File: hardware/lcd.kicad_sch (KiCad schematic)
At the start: 7 parts, among them J3 Conn_01x40, Q2 AO3400A

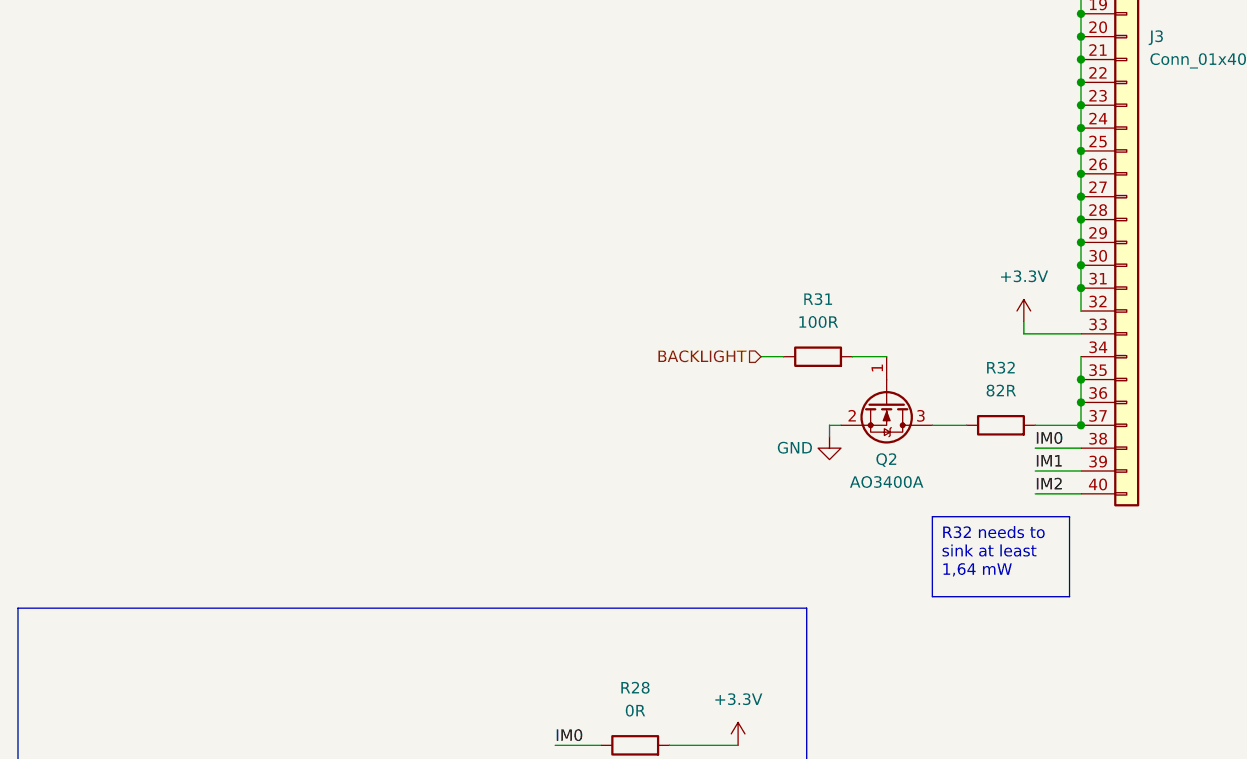
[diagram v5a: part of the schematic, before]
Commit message: Fix resistor value, fix error in schematic
Pin 37 was incorrectly bunched with the backlight LED cathodes, but is
actually a GND pin.
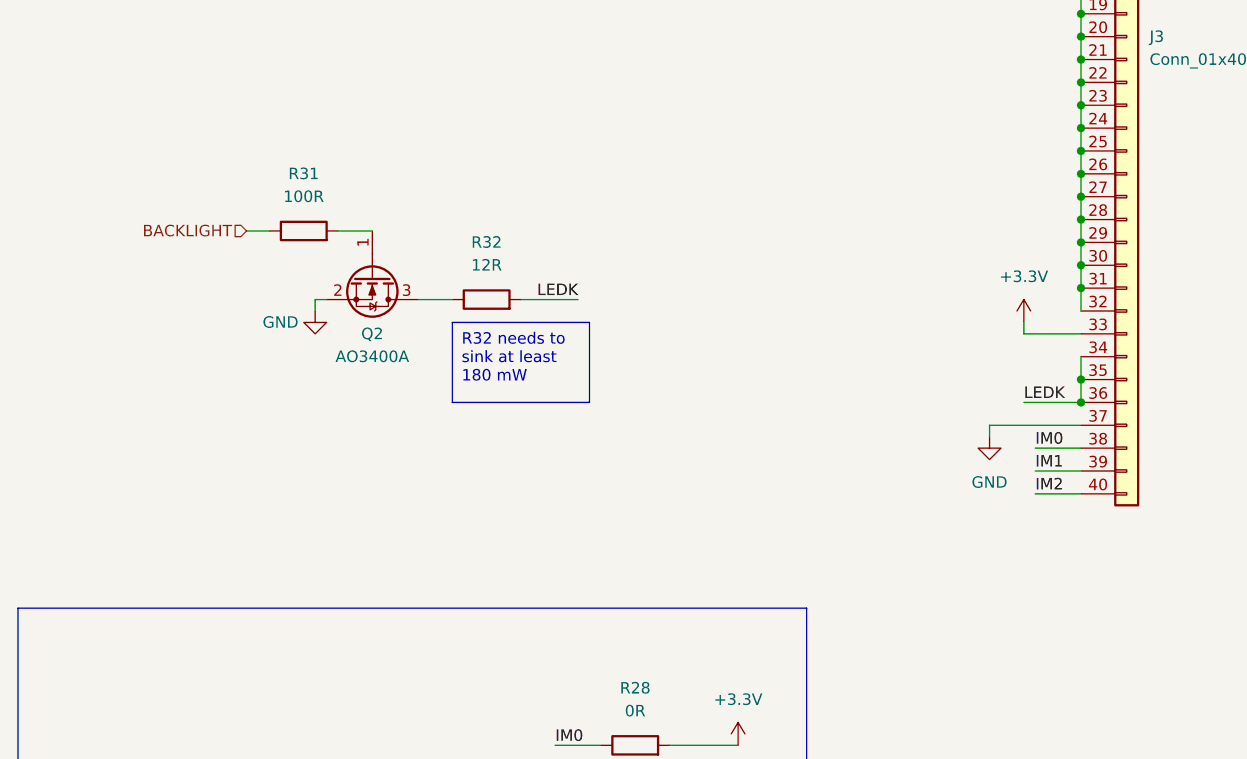
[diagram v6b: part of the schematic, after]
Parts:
- R32: value 82R -> 12R
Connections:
- net GND: now also J3.37 (Pin_37)
- net LEDK: now reaches J3.34 (Pin_34), J3.35 (Pin_35), J3.36 (Pin_36), R32.2
- net LEDK: no longer J3.37 (Pin_37)
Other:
- moved on the sheet: Q2, R31, R32
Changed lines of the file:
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@@
 	)
 	(junction
-		(at 133.35 129.54)
-		(diameter 0)
-		(color 0 0 0 0)
-	)
-	(junction
 		(at 133.35 109.22)
 		(diameter 0)
@@
 	)
 	(junction
-		(at 133.35 127)
+		(at 133.35 99.06)
 		(diameter 0)
 		(color 0 0 0 0)
 	)
 	(junction
-		(at 133.35 99.06)
+		(at 133.35 88.9)
 		(diameter 0)
 		(color 0 0 0 0)
 	)
 	(junction
-		(at 133.35 88.9)
+		(at 133.35 83.82)
 		(diameter 0)
 		(color 0 0 0 0)
 	)
 	(junction
-		(at 133.35 83.82)
+		(at 133.35 127)
 		(diameter 0)
 		(color 0 0 0 0)
@@
 	(wire
 		(pts
+			(xy 71.12 115.57) (xy 77.47 115.57)
+		)
+		(stroke
+			(width 0)
+			(type default)
+		)
+	)
+	(wire
+		(pts
 			(xy 118.11 60.96) (xy 118.11 66.04)
 		)
@@
 	(wire
 		(pts
-			(xy 116.84 129.54) (xy 120.65 129.54)
+			(xy 59.69 115.57) (xy 63.5 115.57)
 		)
 		(stroke
@@
 	(wire
 		(pts
+			(xy 123.19 129.54) (xy 133.35 129.54)
+		)
+		(stroke
+			(width 0)
+			(type default)
+		)
+	)
+	(wire
+		(pts
 			(xy 87.63 185.42) (xy 95.25 185.42)
 		)
@@
 	(wire
 		(pts
+			(xy 123.19 130.81) (xy 123.19 129.54)
+		)
+		(stroke
+			(width 0)
+			(type default)
+		)
+	)
+	(wire
+		(pts
 			(xy 133.35 93.98) (xy 133.35 96.52)
 		)
@@
 	(wire
 		(pts
-			(xy 130.81 55.88) (xy 133.35 55.88)
+			(xy 127 127) (xy 133.35 127)
 		)
 		(stroke
@@
 	(wire
 		(pts
-			(xy 88.9 175.26) (xy 88.9 176.53)
+			(xy 130.81 55.88) (xy 133.35 55.88)
 		)
 		(stroke
@@
 	(wire
 		(pts
-			(xy 87.63 175.26) (xy 88.9 175.26)
+			(xy 88.9 175.26) (xy 88.9 176.53)
 		)
 		(stroke
@@
 	(wire
 		(pts
-			(xy 106.68 129.54) (xy 105.41 129.54)
+			(xy 87.63 175.26) (xy 88.9 175.26)
 		)
 		(stroke
@@
 	(wire
 		(pts
-			(xy 133.35 121.92) (xy 133.35 124.46)
+			(xy 49.53 115.57) (xy 48.26 115.57)
 		)
 		(stroke
@@
 	(wire
 		(pts
-			(xy 133.35 99.06) (xy 133.35 101.6)
+			(xy 133.35 121.92) (xy 133.35 124.46)
 		)
 		(stroke
@@
 	(wire
 		(pts
-			(xy 128.27 132.08) (xy 133.35 132.08)
+			(xy 133.35 99.06) (xy 133.35 101.6)
 		)
 		(stroke
@@
 	(wire
 		(pts
-			(xy 128.27 129.54) (xy 133.35 129.54)
+			(xy 128.27 132.08) (xy 133.35 132.08)
 		)
 		(stroke
@@
 	(wire
 		(pts
-			(xy 133.35 127) (xy 133.35 129.54)
-		)
-		(stroke
-			(width 0)
-			(type default)
-		)
-	)
-	(wire
-		(pts
 			(xy 133.35 124.46) (xy 133.35 127)
 		)
@@
 	(wire
 		(pts
-			(xy 107.95 121.92) (xy 111.76 121.92)
+			(xy 50.8 107.95) (xy 54.61 107.95)
 		)
 		(stroke
@@
 	(wire
 		(pts
-			(xy 105.41 129.54) (xy 105.41 130.81)
+			(xy 48.26 115.57) (xy 48.26 116.84)
 		)
 		(stroke
@@
 	(wire
 		(pts
-			(xy 97.79 121.92) (xy 100.33 121.92)
+			(xy 40.64 107.95) (xy 43.18 107.95)
 		)
 		(stroke
@@
 		)
 	)
-	(text_box "R32 needs to sink at least 1,64 mW"
+	(text_box "R32 needs to sink at least 180 mW"
 		(exclude_from_sim no)
-		(at 116.84 139.7 0)
+		(at 63.5 118.11 0)
 		(size 15.24 8.89)
 		(stroke
@@
 		)
 	)
+	(label "LEDK"
+		(at 77.47 115.57 180)
+		(fields_autoplaced yes)
+		(effects
+			(font
+				(size 1.27 1.27)
+			)
+			(justify right bottom)
+		)
+	)
 	(label "IM2"
 		(at 74.93 185.42 0)
@@
 		)
 	)
+	(label "LEDK"
+		(at 127 127 0)
+		(fields_autoplaced yes)
+		(effects
+			(font
+				(size 1.27 1.27)
+			)
+			(justify left bottom)
+		)
+	)
 	(label "IM1"
 		(at 74.93 175.26 0)
@@
 	(hierarchical_label "BACKLIGHT"
 		(shape input)
-		(at 97.79 121.92 180)
+		(at 40.64 107.95 180)
 		(fields_autoplaced yes)
 		(effects
@@
 	(symbol
 		(lib_id "Device:R")
-		(at 124.46 129.54 90)
+		(at 67.31 115.57 90)
 		(unit 1)
 		(exclude_from_sim no)
@@
 		(fields_autoplaced yes)
 		(property "Reference" "R32"
-			(at 124.46 123.19 90)
+			(at 67.31 109.22 90)
 			(effects
 				(font
@@
 			)
 		)
-		(property "Value" "82R"
-			(at 124.46 125.73 90)
+		(property "Value" "12R"
+			(at 67.31 111.76 90)
 			(effects
 				(font
@@
 		)
 		(property "Footprint" ""
-			(at 124.46 131.318 90)
+			(at 67.31 117.348 90)
 			(effects
 				(font
@@
 		)
 		(property "Datasheet" "~"
-			(at 124.46 129.54 0)
+			(at 67.31 115.57 0)
 			(effects
 				(font
@@
 		)
 		(property "Description" "Resistor"
-			(at 124.46 129.54 0)
+			(at 67.31 115.57 0)
 			(effects
 				(font
@@
 	(symbol
 		(lib_id "power:GND")
-		(at 105.41 130.81 0)
+		(at 48.26 116.84 0)
 		(unit 1)
 		(exclude_from_sim no)
@@
 		(dnp no)
 		(property "Reference" "#PWR068"
-			(at 105.41 137.16 0)
+			(at 48.26 123.19 0)
 			(effects
 				(font
@@
 		)
 		(property "Value" "GND"
-			(at 99.568 132.08 0)
+			(at 42.418 118.11 0)
 			(effects
 				(font
@@
 		)
 		(property "Footprint" ""
-			(at 105.41 130.81 0)
+			(at 48.26 116.84 0)
 			(effects
 				(font
@@
 		)
 		(property "Datasheet" ""
-			(at 105.41 130.81 0)
+			(at 48.26 116.84 0)
 			(effects
 				(font
@@
 		)
 		(property "Description" "Power symbol creates a global label with name \"GND\" , ground"
-			(at 105.41 130.81 0)
+			(at 48.26 116.84 0)
 			(effects
 				(font
@@
 	(symbol
 		(lib_id "power:GND")
+		(at 123.19 130.81 0)
+		(unit 1)
+		(exclude_from_sim no)
+		(in_bom yes)
+		(on_board yes)
+		(dnp no)
+		(fields_autoplaced yes)
+		(property "Reference" "#PWR078"
+			(at 123.19 137.16 0)
+			(effects
+				(font
+					(size 1.27 1.27)
+				)
+				(hide yes)
+			)
+		)
+		(property "Value" "GND"
+			(at 123.19 135.89 0)
+			(effects
+				(font
+					(size 1.27 1.27)
+				)
+			)
+		)
+		(property "Footprint" ""
+			(at 123.19 130.81 0)
+			(effects
+				(font
+					(size 1.27 1.27)
+				)
+				(hide yes)
+			)
+		)
+		(property "Datasheet" ""
+			(at 123.19 130.81 0)
+			(effects
+				(font
+					(size 1.27 1.27)
+				)
+				(hide yes)
+			)
+		)
+		(property "Description" "Power symbol creates a global label with name \"GND\" , ground"
+			(at 123.19 130.81 0)
+			(effects
+				(font
+					(size 1.27 1.27)
+				)
+				(hide yes)
+			)
+		)
+		(pin "1"
+		)
+		(instances
+			(project "badge"
+				(path "/dc4a3d77-b0f8-4e90-a4be-3e93c7025348/ce5aa0f6-0554-44ba-9e09-c73e868ec9d0"
+					(reference "#PWR078")
+					(unit 1)
+				)
+			)
+		)
+	)
+	(symbol
+		(lib_id "power:GND")
 		(at 133.35 48.26 270)
 		(unit 1)
@@
 	(symbol
 		(lib_id "Device:R")
-		(at 104.14 121.92 90)
+		(at 46.99 107.95 90)
 		(unit 1)
 		(exclude_from_sim no)
@@
 		(fields_autoplaced yes)
 		(property "Reference" "R31"
-			(at 104.14 115.57 90)
+			(at 46.99 101.6 90)
 			(effects
 				(font
@@
 		)
 		(property "Value" "100R"
-			(at 104.14 118.11 90)
+			(at 46.99 104.14 90)
 			(effects
 				(font
@@
 		)
 		(property "Footprint" ""
-			(at 104.14 123.698 90)
+			(at 46.99 109.728 90)
 			(effects
 				(font
@@
 		)
 		(property "Datasheet" "~"
-			(at 104.14 121.92 0)
+			(at 46.99 107.95 0)
 			(effects
 				(font
@@
 		)
 		(property "Description" "Resistor"
-			(at 104.14 121.92 0)
+			(at 46.99 107.95 0)
 			(effects
 				(font
@@
 	(symbol
 		(lib_id "Transistor_FET:AO3400A")
-		(at 111.76 127 270)
+		(at 54.61 113.03 270)
 		(unit 1)
 		(exclude_from_sim no)
@@
 		(fields_autoplaced yes)
 		(property "Reference" "Q2"
-			(at 111.76 133.35 90)
+			(at 54.61 119.38 90)
 			(effects
 				(font
@@
 		)
 		(property "Value" "AO3400A"
-			(at 111.76 135.89 90)
+			(at 54.61 121.92 90)
 			(effects
 				(font
@@
 		)
 		(property "Footprint" "Package_TO_SOT_SMD:SOT-23"
-			(at 109.855 132.08 0)
+			(at 52.705 118.11 0)
 			(effects
 				(font
@@
 		)
 		(property "Datasheet" "http://www.aosmd.com/pdfs/datasheet/AO3400A.pdf"
-			(at 107.95 132.08 0)
+			(at 50.8 118.11 0)
 			(effects
 				(font
@@
 		)
 		(property "Description" "30V Vds, 5.7A Id, N-Channel MOSFET, SOT-23"
-			(at 111.76 127 0)
+			(at 54.61 113.03 0)
 			(effects
 				(font

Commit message: use AO3400A in place of the npn
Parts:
- removed Q2: AO3400A, Package_TO_SOT_SMD:SOT-23, symbol Transistor_FET:AO3400A
- added Q3: AO3400A, Package_TO_SOT_SMD:SOT-23, symbol Transistor_FET:AO3400A
- R28: footprint (none) -> lib:SKRHABE010_ALPS
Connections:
- net GND: now also Q3.2 (S)
- net at R32.1: now also Q3.3 (D)
- net at R31.2: now also Q3.1 (G)
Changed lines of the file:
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@@
+	)
+	(symbol
+		(lib_id "Transistor_FET:AO3400A")
+		(at 54.61 113.03 270)
+		(unit 1)
+		(exclude_from_sim no)
+		(in_bom yes)
+		(on_board yes)
+		(dnp no)
+		(fields_autoplaced yes)
+		(property "Reference" "Q3"
+			(at 54.61 119.38 90)
+			(effects
+				(font
+					(size 1.27 1.27)
+				)
+			)
+		)
+		(property "Value" "AO3400A"
+			(at 54.61 121.92 90)
+			(effects
+				(font
+					(size 1.27 1.27)
+				)
+			)
+		)
+		(property "Footprint" "Package_TO_SOT_SMD:SOT-23"
+			(at 52.705 118.11 0)
+			(effects
+				(font
+					(size 1.27 1.27)
+					(italic yes)
+				)
+				(justify left)
+				(hide yes)
+			)
+		)
+		(property "Datasheet" "http://www.aosmd.com/pdfs/datasheet/AO3400A.pdf"
+			(at 50.8 118.11 0)
+			(effects
+				(font
+					(size 1.27 1.27)
+				)
+				(justify left)
+				(hide yes)
+			)
+		)
+		(property "Description" "30V Vds, 5.7A Id, N-Channel MOSFET, SOT-23"
+			(at 54.61 113.03 0)
+			(effects
+				(font
+					(size 1.27 1.27)
+				)
+				(hide yes)
+			)
+		)
+		(property "LCSC" "C20917"
+			(at 54.61 113.03 0)
+			(effects
+				(font
+					(size 1.27 1.27)
+				)
+				(hide yes)
+			)
+		)
+		(pin "1"
+		)
+		(pin "2"
+		)
+		(pin "3"
+		)
+		(instances
+			(project "badge"
+				(path "/dc4a3d77-b0f8-4e90-a4be-3e93c7025348/ce5aa0f6-0554-44ba-9e09-c73e868ec9d0"
+					(reference "Q3")
+					(unit 1)
+				)
+			)
+		)
 	)
 	(symbol
@@
 			)
 		)
-		(property "Footprint" ""
+		(property "Footprint" "lib:SKRHABE010_ALPS"
 			(at 83.82 166.878 90)
 			(effects
@@
 					(unit 1)
 				)
-			)
-		)
-	)
-	(symbol
-		(lib_id "Transistor_FET:AO3400A")
-		(at 54.61 113.03 270)
-		(unit 1)
-		(exclude_from_sim no)
-		(in_bom yes)
-		(on_board yes)
-		(dnp no)
-		(fields_autoplaced yes)
-		(property "Reference" "Q2"
-			(at 54.61 119.38 90)
-			(effects
-				(font
-					(size 1.27 1.27)
-				)
-			)
-		)
-		(property "Value" "AO3400A"
-			(at 54.61 121.92 90)
-			(effects
-				(font
-					(size 1.27 1.27)
-				)
-			)
-		)
-		(property "Footprint" "Package_TO_SOT_SMD:SOT-23"
-			(at 52.705 118.11 0)
-			(effects
-				(font
-					(size 1.27 1.27)
-					(italic yes)
-				)
-				(justify left)
-				(hide yes)
-			)
-		)
-		(property "Datasheet" "http://www.aosmd.com/pdfs/datasheet/AO3400A.pdf"
-			(at 50.8 118.11 0)
-			(effects
-				(font
-					(size 1.27 1.27)
-				)
-				(justify left)
-				(hide yes)
-			)
-		)
-		(property "Description" "30V Vds, 5.7A Id, N-Channel MOSFET, SOT-23"
-			(at 54.61 113.03 0)
-			(effects
-				(font
-					(size 1.27 1.27)
-				)
-				(hide yes)
-			)
-		)
-		(pin "1"
-		)
-		(pin "2"
-		)
-		(pin "3"
-		)
-		(instances
-			(project "badge"
-				(path "/dc4a3d77-b0f8-4e90-a4be-3e93c7025348/ce5aa0f6-0554-44ba-9e09-c73e868ec9d0"
-					(reference "Q2")
-					(unit 1)
-				)

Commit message: remove lcd reset short circuit to gnd
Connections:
- net GND: no longer J3.15 (Pin_15)
- new net RESET: J3.15 (Pin_15)
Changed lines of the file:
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@@
-	)
-	(junction
-		(at 133.35 73.66)
-		(diameter 0)
-		(color 0 0 0 0)
 	)
 	(junction
@@
 		)
 		(stroke
-			(width 0)
-			(type default)
-		)
-	)
-	(wire
-		(pts
-			(xy 133.35 76.2) (xy 133.35 73.66)
-		)
-		(stroke
